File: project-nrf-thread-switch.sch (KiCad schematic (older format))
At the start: 2 parts

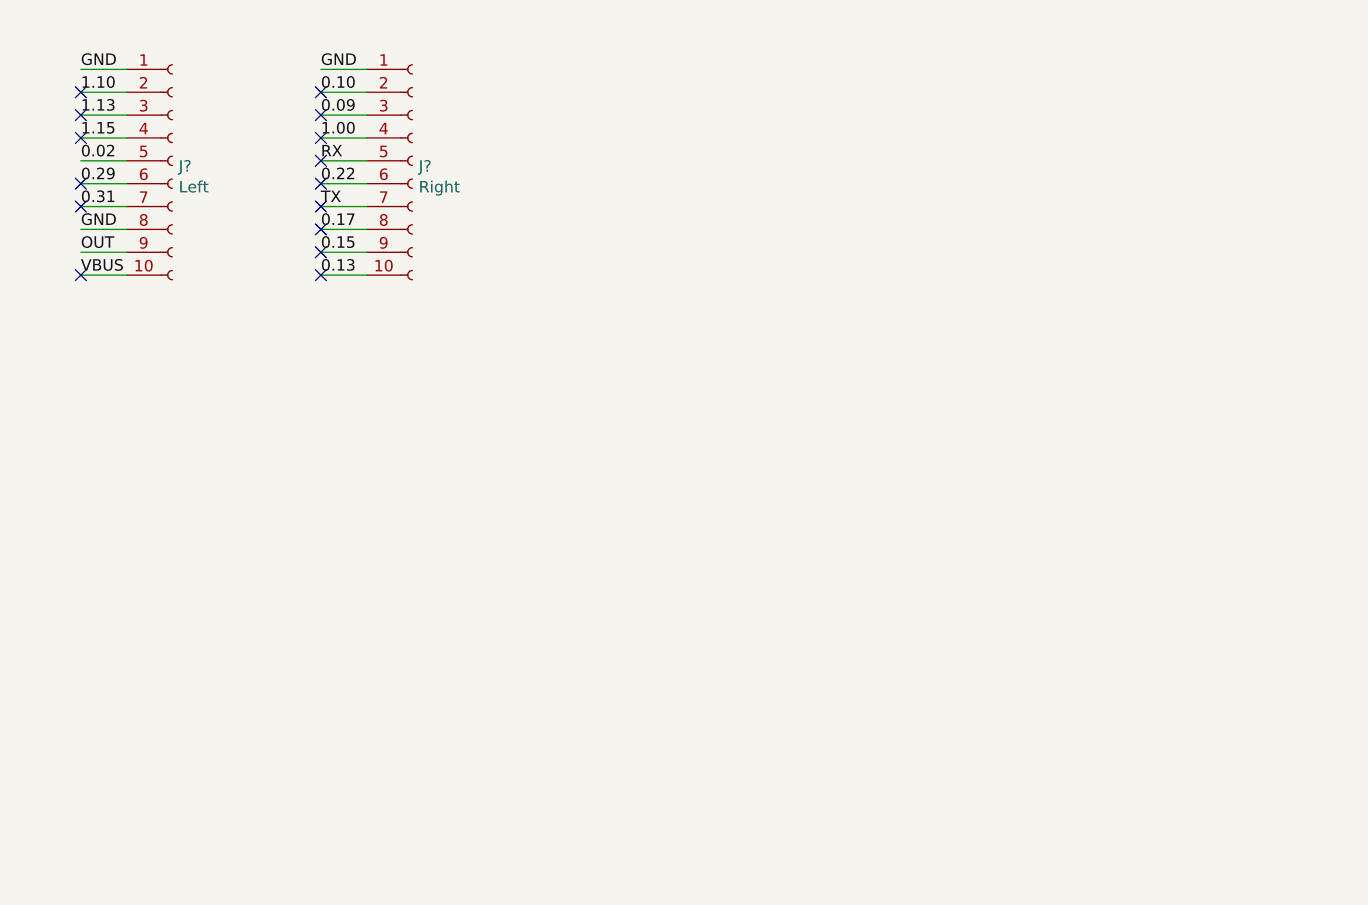
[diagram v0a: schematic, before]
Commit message: Add 8 buttons and the battery
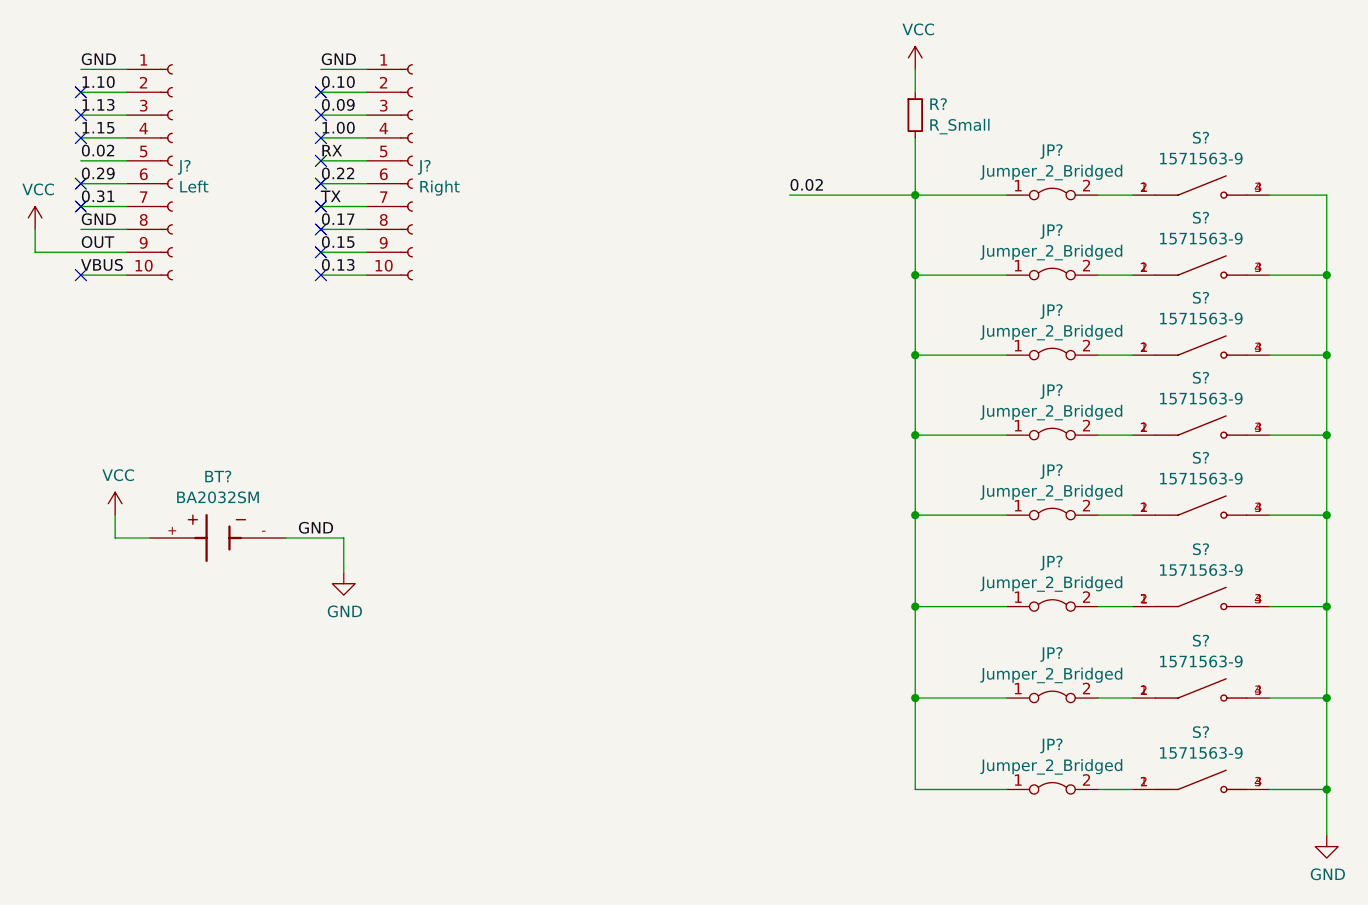
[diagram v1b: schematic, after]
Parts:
- added BT?: BA2032SM, BAT_BA2032SM, symbol BA2032SM:BA2032SM
- added JP? (x8): Jumper_2_Bridged, Jumper:SolderJumper-2_P1.3mm_Bridged_RoundedPad1.0x1.5mm, symbol Jumper:Jumper_2_Bridged
- added R?: R_Small, symbol Device:R_Small
- added S? (x8): 1571563-9, SW_1571563-9, symbol 1571563-9:1571563-9
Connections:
- net 0.02: now also JP?.1 (A), JP?.1 (A), JP?.1 (A), JP?.1 (A), JP?.1 (A), JP?.1 (A), JP?.1 (A), JP?.1 (A), R?.2
- net GND: now also BT?.-, S?.3, S?.3, S?.3, S?.3, S?.3, S?.3, S?.3, S?.3, S?.4, S?.4, S?.4, S?.4, S?.4, S?.4, S?.4, S?.4
- net OUT renamed VCC
- net VCC: now also BT?.+, R?.1
- new net: JP?.2 (B), S?.1, S?.2 (x8)

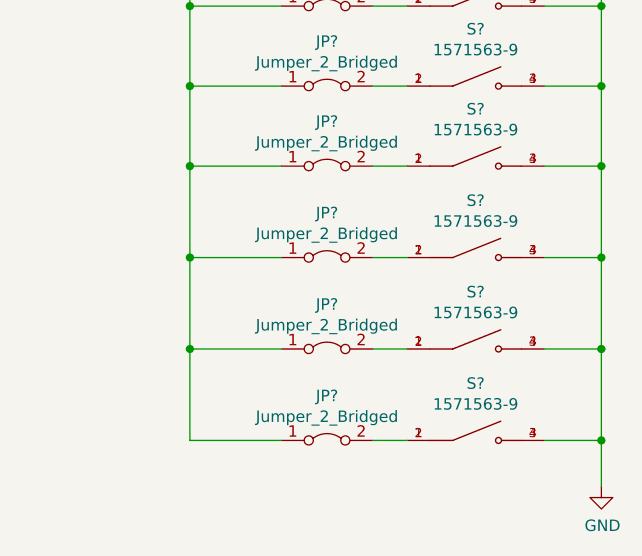
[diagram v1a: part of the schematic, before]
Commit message: Keep 5 buttons
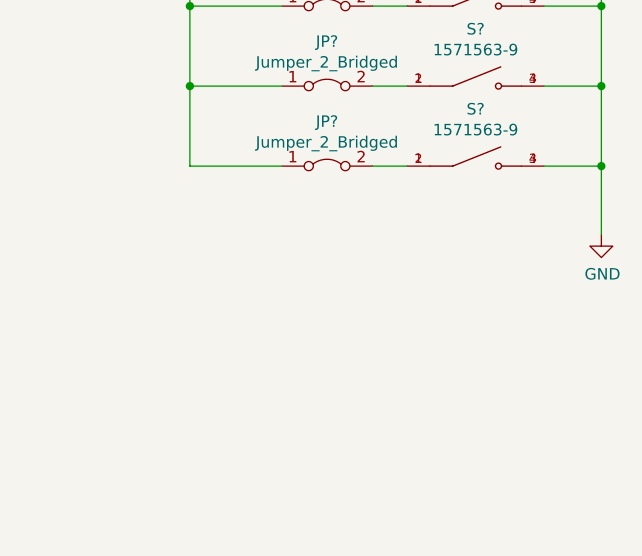
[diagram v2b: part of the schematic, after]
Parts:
- removed JP? (x3): Jumper_2_Bridged, Jumper:SolderJumper-2_P1.3mm_Bridged_RoundedPad1.0x1.5mm, symbol Jumper:Jumper_2_Bridged
- removed S? (x3): 1571563-9, SW_1571563-9, symbol 1571563-9:1571563-9
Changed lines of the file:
@@
-$EndComp
-$Comp
-L 1571563-9:1571563-9 S?
-U 1 1 62331153
-P 6200 3750
-F 0 "S?" H 6200 3999 50  0000 C CNN
-F 1 "1571563-9" H 6200 3908 50  0000 C CNN
-F 2 "SW_1571563-9" H 6200 3750 50  0001 L BNN
-F 3 "" H 6200 3750 50  0001 L BNN
-F 4 "Compliant" H 6200 3750 50  0001 L BNN "EU_RoHS_Compliance"
-F 5 "1571563-9" H 6200 3750 50  0001 L BNN "Comment"
-	1    6200 3750
-	1    0    0    -1
-$EndComp
-$Comp
-L 1571563-9:1571563-9 S?
-U 1 1 62331988
-P 6200 4150
-F 0 "S?" H 6200 4399 50  0000 C CNN
-F 1 "1571563-9" H 6200 4308 50  0000 C CNN
-F 2 "SW_1571563-9" H 6200 4150 50  0001 L BNN
-F 3 "" H 6200 4150 50  0001 L BNN
-F 4 "Compliant" H 6200 4150 50  0001 L BNN "EU_RoHS_Compliance"
-F 5 "1571563-9" H 6200 4150 50  0001 L BNN "Comment"
-	1    6200 4150
-	1    0    0    -1
-$EndComp
-$Comp
-L 1571563-9:1571563-9 S?
-U 1 1 6233240E
-P 6200 4550
-F 0 "S?" H 6200 4799 50  0000 C CNN
-F 1 "1571563-9" H 6200 4708 50  0000 C CNN
-F 2 "SW_1571563-9" H 6200 4550 50  0001 L BNN
-F 3 "" H 6200 4550 50  0001 L BNN
-F 4 "Compliant" H 6200 4550 50  0001 L BNN "EU_RoHS_Compliance"
-F 5 "1571563-9" H 6200 4550 50  0001 L BNN "Comment"
-	1    6200 4550
-	1    0    0    -1
 $EndComp
 $Comp
@@
 L power:GND #PWR?
 U 1 1 6234D28E
-P 6750 4750
-F 0 "#PWR?" H 6750 4500 50  0001 C CNN
-F 1 "GND" H 6755 4577 50  0000 C CNN
-F 2 "" H 6750 4750 50  0001 C CNN
-F 3 "" H 6750 4750 50  0001 C CNN
-	1    6750 4750
-	1    0    0    -1
-$EndComp
-Wire Wire Line
-	6500 4550 6750 4550
-Wire Wire Line
-	6750 4550 6750 4750
+P 6750 3650
+F 0 "#PWR?" H 6750 3400 50  0001 C CNN
+F 1 "GND" H 6755 3477 50  0000 C CNN
+F 2 "" H 6750 3650 50  0001 C CNN
+F 3 "" H 6750 3650 50  0001 C CNN
+	1    6750 3650
+	1    0    0    -1
+$EndComp
 Wire Wire Line
 	6500 2650 6750 2650
 Wire Wire Line
 	6750 2650 6750 3000
-Connection ~ 6750 4550
 Wire Wire Line
 	6750 3000 6500 3000
@@
 Wire Wire Line
 	6750 3350 6500 3350
-Connection ~ 6750 3350
-Wire Wire Line
-	6750 3350 6750 3750
-Wire Wire Line
-	6750 3750 6500 3750
-Connection ~ 6750 3750
-Wire Wire Line
-	6750 3750 6750 4150
-Wire Wire Line
-	6750 4150 6500 4150
-Connection ~ 6750 4150
-Wire Wire Line
-	6750 4150 6750 4550
 Text Label 4400 1950 0    50   ~ 0
 0.02
@@
 F 3 "~" H 5550 3350 50  0001 C CNN
 	1    5550 3350
-	1    0    0    -1
-$EndComp
-$Comp
-L Jumper:Jumper_2_Bridged JP?
-U 1 1 6235DA08
-P 5550 3750
-F 0 "JP?" H 5550 3945 50  0000 C CNN
-F 1 "Jumper_2_Bridged" H 5550 3854 50  0000 C CNN
-F 2 "Jumper:SolderJumper-2_P1.3mm_Bridged_RoundedPad1.0x1.5mm" H 5550 3750 50  0001 C CNN
-F 3 "~" H 5550 3750 50  0001 C CNN
-	1    5550 3750
-	1    0    0    -1
-$EndComp
-$Comp
-L Jumper:Jumper_2_Bridged JP?
-U 1 1 6235DFD0
-P 5550 4150
-F 0 "JP?" H 5550 4345 50  0000 C CNN
-F 1 "Jumper_2_Bridged" H 5550 4254 50  0000 C CNN
-F 2 "Jumper:SolderJumper-2_P1.3mm_Bridged_RoundedPad1.0x1.5mm" H 5550 4150 50  0001 C CNN
-F 3 "~" H 5550 4150 50  0001 C CNN
-	1    5550 4150
-	1    0    0    -1
-$EndComp
-$Comp
-L Jumper:Jumper_2_Bridged JP?
-U 1 1 6235E630
-P 5550 4550
-F 0 "JP?" H 5550 4745 50  0000 C CNN
-F 1 "Jumper_2_Bridged" H 5550 4654 50  0000 C CNN
-F 2 "Jumper:SolderJumper-2_P1.3mm_Bridged_RoundedPad1.0x1.5mm" H 5550 4550 50  0001 C CNN
-F 3 "~" H 5550 4550 50  0001 C CNN
-	1    5550 4550
 	1    0    0    -1
 $EndComp
@@
 	5900 3350 5750 3350
 Wire Wire Line
-	5750 3750 5900 3750
-Wire Wire Line
-	5900 4150 5750 4150
-Wire Wire Line
-	5750 4550 5900 4550
-Wire Wire Line
 	4950 1400 4950 1500
 Wire Wire Line
@@
 Wire Wire Line
 	4950 2300 4950 2650
-Wire Wire Line
-	4950 4150 5350 4150
 Connection ~ 4950 2300
 Wire Wire Line
@@
 Wire Wire Line
 	5350 3350 4950 3350
-Connection ~ 4950 3350
-Wire Wire Line
-	4950 3350 4950 3750
-Wire Wire Line
-	5350 3750 4950 3750
-Connection ~ 4950 3750
-Wire Wire Line
-	4950 3750 4950 4150
-Wire Wire Line
-	5350 4550 4950 4550
-Wire Wire Line
-	4950 4550 4950 4150
-Connection ~ 4950 4150
+Wire Wire Line
+	6750 3650 6750 3350
+Connection ~ 6750 3350
 $EndSCHEMATC

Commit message: First routing
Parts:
- R1: renamed from R?; footprint (none) -> Resistor_SMD:R_0603_1608Metric
- gave numbers to parts that had none: 13
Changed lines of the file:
@@
 $EndDescr
 $Comp
-L Connector:Conn_01x10_Female J?
+L Connector:Conn_01x10_Female J1
 U 1 1 62320CB9
 P 1700 1800
-F 0 "J?" H 1728 1776 50  0000 L CNN
+F 0 "J1" H 1728 1776 50  0000 L CNN
 F 1 "Left" H 1728 1685 50  0000 L CNN
 F 2 "Connector_PinSocket_2.54mm:PinSocket_1x10_P2.54mm_Vertical_SMD_Pin1Left" H 1700 1800 50  0001 C CNN
@@
 $EndComp
 $Comp
-L Connector:Conn_01x10_Female J?
+L Connector:Conn_01x10_Female J2
 U 1 1 62321C96
 P 2750 1800
-F 0 "J?" H 2778 1776 50  0000 L CNN
+F 0 "J2" H 2778 1776 50  0000 L CNN
 F 1 "Right" H 2778 1685 50  0000 L CNN
 F 2 "Connector_PinSocket_2.54mm:PinSocket_1x10_P2.54mm_Vertical_SMD_Pin1Left" H 2750 1800 50  0001 C CNN
@@
 NoConn ~ 2350 2300
 $Comp
-L 1571563-9:1571563-9 S?
+L 1571563-9:1571563-9 S3
 U 1 1 6232D2C3
 P 6200 2650
-F 0 "S?" H 6200 2899 50  0000 C CNN
+F 0 "S3" H 6200 2899 50  0000 C CNN
 F 1 "1571563-9" H 6200 2808 50  0000 C CNN
 F 2 "SW_1571563-9" H 6200 2650 50  0001 L BNN
@@
 $EndComp
 $Comp
-L 1571563-9:1571563-9 S?
+L 1571563-9:1571563-9 S4
 U 1 1 62330650
 P 6200 3000
-F 0 "S?" H 6200 3249 50  0000 C CNN
+F 0 "S4" H 6200 3249 50  0000 C CNN
 F 1 "1571563-9" H 6200 3158 50  0000 C CNN
 F 2 "SW_1571563-9" H 6200 3000 50  0001 L BNN
@@
 $EndComp
 $Comp
-L 1571563-9:1571563-9 S?
+L 1571563-9:1571563-9 S5
 U 1 1 62330C79
 P 6200 3350
-F 0 "S?" H 6200 3599 50  0000 C CNN
+F 0 "S5" H 6200 3599 50  0000 C CNN
 F 1 "1571563-9" H 6200 3508 50  0000 C CNN
 F 2 "SW_1571563-9" H 6200 3350 50  0001 L BNN
@@
 $EndComp
 $Comp
-L BA2032SM:BA2032SM BT?
+L BA2032SM:BA2032SM BT1
 U 1 1 623369E5
 P 1900 3450
-F 0 "BT?" H 1900 3717 50  0000 C CNN
+F 0 "BT1" H 1900 3717 50  0000 C CNN
 F 1 "BA2032SM" H 1900 3626 50  0000 C CNN
 F 2 "BAT_BA2032SM" H 1900 3450 50  0001 L BNN
@@
 $EndComp
 $Comp
-L power:VCC #PWR?
+L power:VCC #PWR0101
 U 1 1 6233943D
 P 1450 3350
-F 0 "#PWR?" H 1450 3200 50  0001 C CNN
+F 0 "#PWR0101" H 1450 3200 50  0001 C CNN
 F 1 "VCC" H 1465 3523 50  0000 C CNN
 F 2 "" H 1450 3350 50  0001 C CNN
@@
 $EndComp
 $Comp
-L power:GND #PWR?
+L power:GND #PWR0102
 U 1 1 62339B1A
 P 2450 3600
-F 0 "#PWR?" H 2450 3350 50  0001 C CNN
+F 0 "#PWR0102" H 2450 3350 50  0001 C CNN
 F 1 "GND" H 2455 3427 50  0000 C CNN
 F 2 "" H 2450 3600 50  0001 C CNN
@@
 GND
 $Comp
-L power:VCC #PWR?
+L power:VCC #PWR0103
 U 1 1 6234B506
 P 1100 2100
-F 0 "#PWR?" H 1100 1950 50  0001 C CNN
+F 0 "#PWR0103" H 1100 1950 50  0001 C CNN
 F 1 "VCC" H 1115 2273 50  0000 C CNN
 F 2 "" H 1100 2100 50  0001 C CNN
@@
 	1100 2200 1500 2200
 $Comp
-L power:GND #PWR?
+L power:GND #PWR0104
 U 1 1 6234D28E
 P 6750 3650
-F 0 "#PWR?" H 6750 3400 50  0001 C CNN
+F 0 "#PWR0104" H 6750 3400 50  0001 C CNN
 F 1 "GND" H 6755 3477 50  0000 C CNN
 F 2 "" H 6750 3650 50  0001 C CNN
@@
 0.02
 $Comp
-L Device:R_Small R?
+L Device:R_Small R1
 U 1 1 62359C57
 P 4950 1600
-F 0 "R?" H 5009 1646 50  0000 L CNN
+F 0 "R1" H 5009 1646 50  0000 L CNN
 F 1 "R_Small" H 5009 1555 50  0000 L CNN
-F 2 "" H 4950 1600 50  0001 C CNN
+F 2 "Resistor_SMD:R_0603_1608Metric" H 4950 1600 50  0001 C CNN
 F 3 "~" H 4950 1600 50  0001 C CNN
 	1    4950 1600
@@
 $EndComp
 $Comp
-L power:VCC #PWR?
+L power:VCC #PWR0105
 U 1 1 6235A371
 P 4950 1400
-F 0 "#PWR?" H 4950 1250 50  0001 C CNN
+F 0 "#PWR0105" H 4950 1250 50  0001 C CNN
 F 1 "VCC" H 4965 1573 50  0000 C CNN
 F 2 "" H 4950 1400 50  0001 C CNN
@@
 $EndComp
 $Comp
-L Jumper:Jumper_2_Bridged JP?
+L Jumper:Jumper_2_Bridged JP3
 U 1 1 6235C81B
 P 5550 2650
-F 0 "JP?" H 5550 2845 50  0000 C CNN
+F 0 "JP3" H 5550 2845 50  0000 C CNN
 F 1 "Jumper_2_Bridged" H 5550 2754 50  0000 C CNN
 F 2 "Jumper:SolderJumper-2_P1.3mm_Bridged_RoundedPad1.0x1.5mm" H 5550 2650 50  0001 C CNN
@@
 $EndComp
 $Comp
-L Jumper:Jumper_2_Bridged JP?
+L Jumper:Jumper_2_Bridged JP4
 U 1 1 6235CF48
 P 5550 3000
-F 0 "JP?" H 5550 3195 50  0000 C CNN
+F 0 "JP4" H 5550 3195 50  0000 C CNN
 F 1 "Jumper_2_Bridged" H 5550 3104 50  0000 C CNN
 F 2 "Jumper:SolderJumper-2_P1.3mm_Bridged_RoundedPad1.0x1.5mm" H 5550 3000 50  0001 C CNN
@@
 $EndComp
 $Comp
-L Jumper:Jumper_2_Bridged JP?
+L Jumper:Jumper_2_Bridged JP5
 U 1 1 6235D4BC
 P 5550 3350
-F 0 "JP?" H 5550 3545 50  0000 C CNN
+F 0 "JP5" H 5550 3545 50  0000 C CNN
 F 1 "Jumper_2_Bridged" H 5550 3454 50  0000 C CNN
 F 2 "Jumper:SolderJumper-2_P1.3mm_Bridged_RoundedPad1.0x1.5mm" H 5550 3350 50  0001 C CNN
@@
 $EndComp
 $Comp
-L 1571563-9:1571563-9 S?
+L 1571563-9:1571563-9 S1
 U 1 1 6236F713
 P 6200 1950
-F 0 "S?" H 6200 2199 50  0000 C CNN
+F 0 "S1" H 6200 2199 50  0000 C CNN
 F 1 "1571563-9" H 6200 2108 50  0000 C CNN
 F 2 "SW_1571563-9" H 6200 1950 50  0001 L BNN
@@
 $EndComp
 $Comp
-L 1571563-9:1571563-9 S?
+L 1571563-9:1571563-9 S2
 U 1 1 6236F71B
 P 6200 2300
-F 0 "S?" H 6200 2549 50  0000 C CNN
+F 0 "S2" H 6200 2549 50  0000 C CNN
 F 1 "1571563-9" H 6200 2458 50  0000 C CNN
 F 2 "SW_1571563-9" H 6200 2300 50  0001 L BNN
@@
 	6750 2300 6500 2300
 $Comp
-L Jumper:Jumper_2_Bridged JP?
+L Jumper:Jumper_2_Bridged JP1
 U 1 1 6236F726
 P 5550 1950
-F 0 "JP?" H 5550 2145 50  0000 C CNN
+F 0 "JP1" H 5550 2145 50  0000 C CNN
 F 1 "Jumper_2_Bridged" H 5550 2054 50  0000 C CNN
 F 2 "Jumper:SolderJumper-2_P1.3mm_Bridged_RoundedPad1.0x1.5mm" H 5550 1950 50  0001 C CNN
@@
 $EndComp
 $Comp
-L Jumper:Jumper_2_Bridged JP?
+L Jumper:Jumper_2_Bridged JP2
 U 1 1 6236F72C
 P 5550 2300
-F 0 "JP?" H 5550 2495 50  0000 C CNN
+F 0 "JP2" H 5550 2495 50  0000 C CNN
 F 1 "Jumper_2_Bridged" H 5550 2404 50  0000 C CNN
 F 2 "Jumper:SolderJumper-2_P1.3mm_Bridged_RoundedPad1.0x1.5mm" H 5550 2300 50  0001 C CNN
